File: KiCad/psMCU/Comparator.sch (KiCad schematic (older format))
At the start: 4 parts

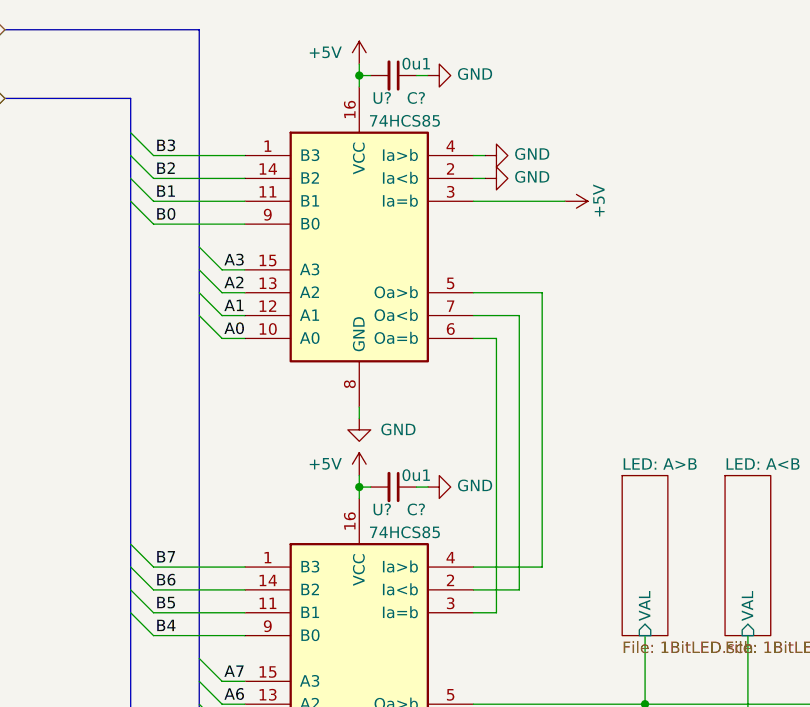
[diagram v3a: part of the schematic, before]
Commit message: Added some footprints, small optimisations
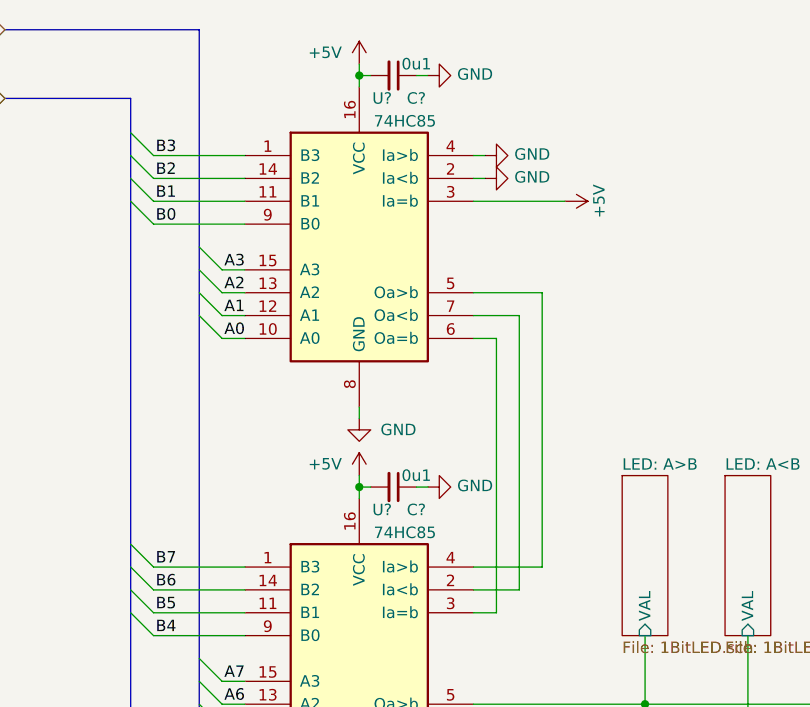
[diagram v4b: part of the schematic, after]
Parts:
- U? (x2): value 74HCS85 -> 74HC85; footprint (none) -> Package_SO:SOIC-16W_5.3x10.2mm_P1.27mm
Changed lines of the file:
@@
 AR Path="/5FD6B215/60020E04" Ref="U?"  Part="1"
 F 0 "U?" H 5600 4150 50  0000 C CNN
-F 1 "74HCS85" H 5700 4050 50  0000 C CNN
-F 2 "" H 5500 3500 50  0001 C CNN
+F 1 "74HC85" H 5700 4050 50  0000 C CNN
+F 2 "Package_SO:SOIC-16W_5.3x10.2mm_P1.27mm" H 5500 3500 50  0001 C CNN
 F 3 "http://www.ti.com/lit/gpn/sn74LS85" H 5500 3500 50  0001 C CNN
 	1    5500 3500
@@
 AR Path="/5FD6B215/60020521" Ref="U?"  Part="1"
 F 0 "U?" H 5600 2350 50  0000 C CNN
-F 1 "74HCS85" H 5700 2250 50  0000 C CNN
-F 2 "" H 5500 1700 50  0001 C CNN
+F 1 "74HC85" H 5700 2250 50  0000 C CNN
+F 2 "Package_SO:SOIC-16W_5.3x10.2mm_P1.27mm" H 5500 1700 50  0001 C CNN
 F 3 "http://www.ti.com/lit/gpn/sn74LS85" H 5500 1700 50  0001 C CNN
 	1    5500 1700

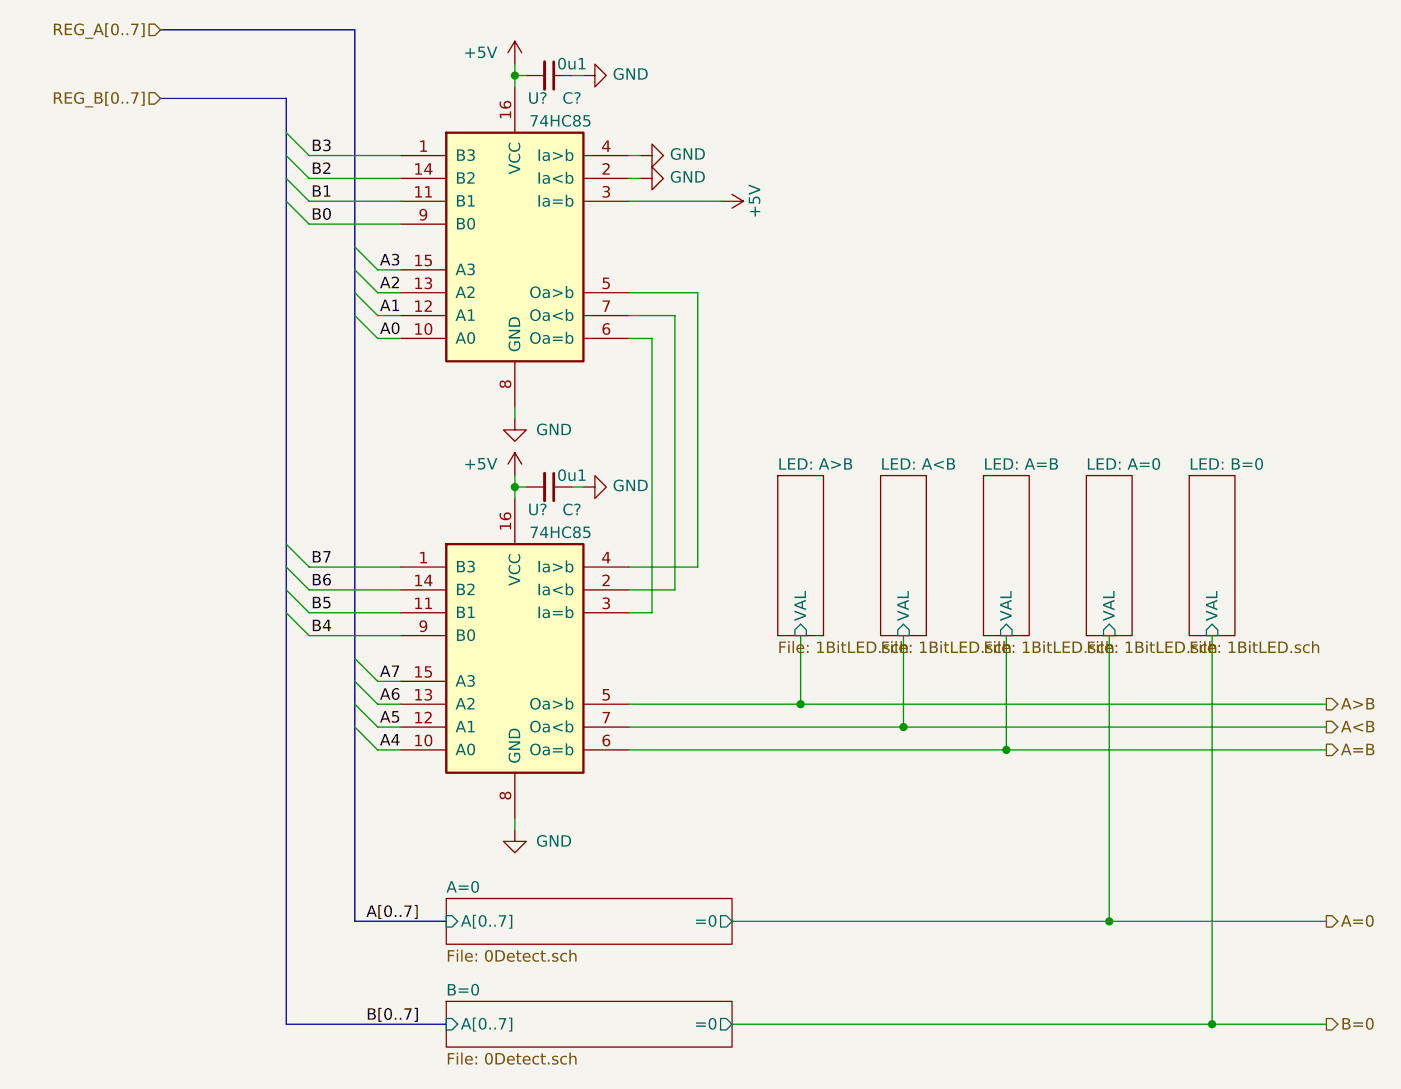
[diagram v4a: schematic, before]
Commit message: Removed Single LED sheets
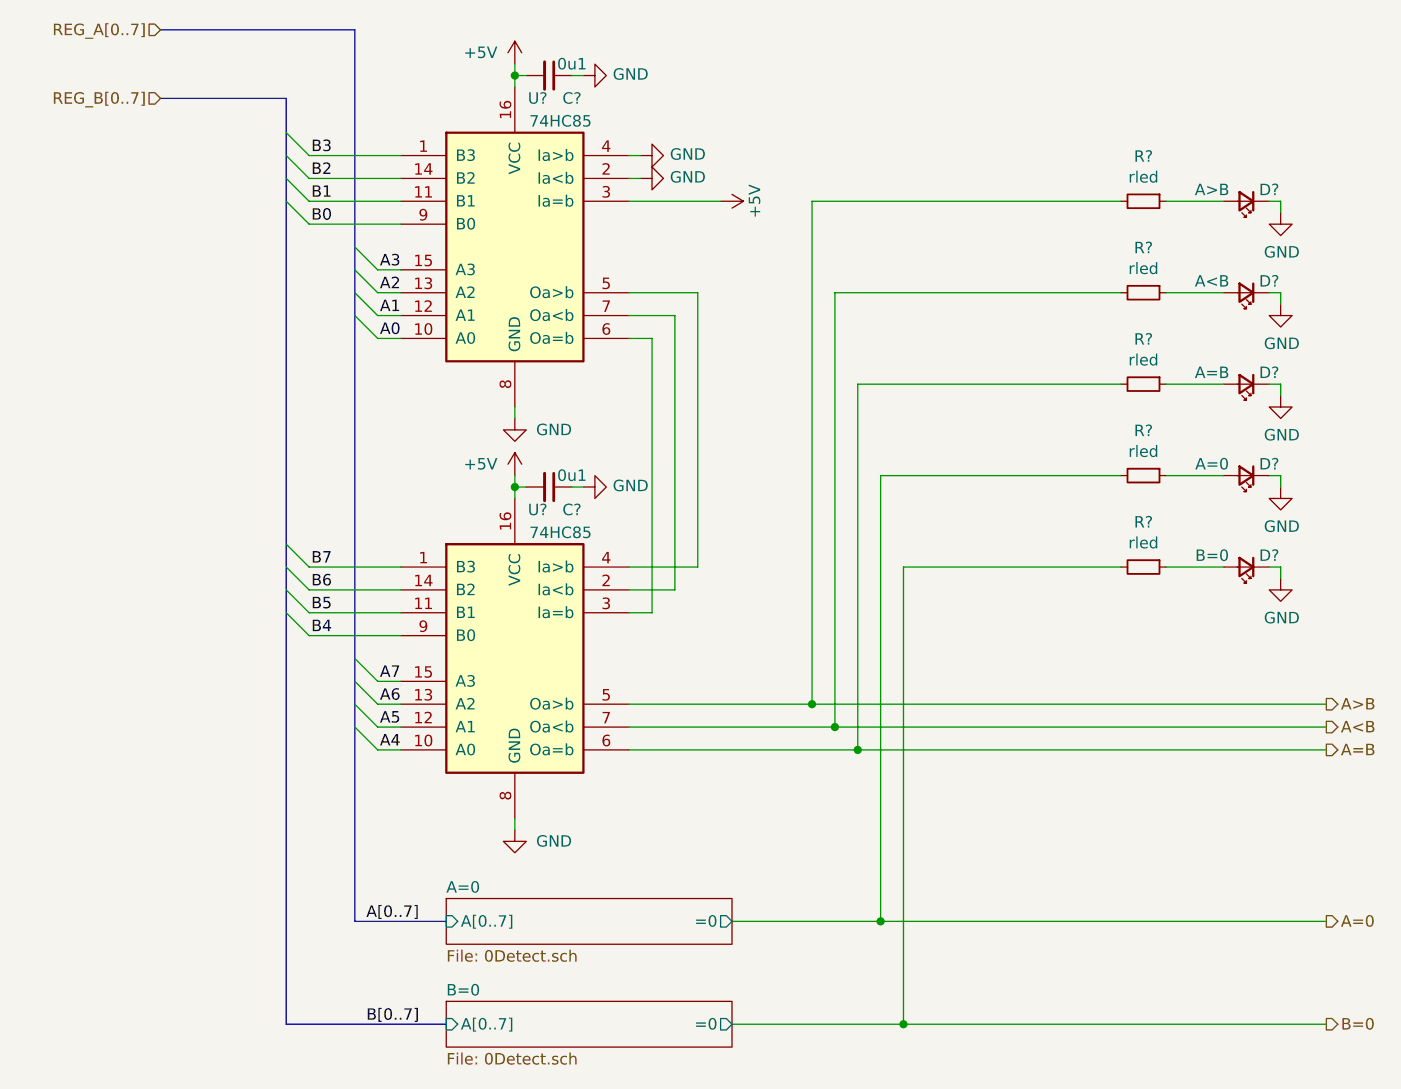
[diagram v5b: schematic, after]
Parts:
- added D?: A<B, Diode_SMD:D_0603_1608Metric, symbol Device:LED_Small
- added D?: A=B, Diode_SMD:D_0603_1608Metric, symbol Device:LED_Small
- added D?: A=0, Diode_SMD:D_0603_1608Metric, symbol Device:LED_Small
- added D?: B=0, Diode_SMD:D_0603_1608Metric, symbol Device:LED_Small
- added D?: A>B, Diode_SMD:D_0603_1608Metric, symbol Device:LED_Small
- added R? (x5): rled, Resistor_SMD:R_0603_1608Metric, symbol Device:R_Small
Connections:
- net A<B: now also R?.2
- net A=0: now also R?.2
- net A=B: now also R?.2
- net A>B: now also R?.2
- net B=0: now also R?.2
- net GND: now also D?.1 (K), D?.1 (K), D?.1 (K), D?.1 (K), D?.1 (K)
- new net: D?.2 (A), R?.1 (x5)

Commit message: First Schematic Draft done.
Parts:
- C210, C211: renamed from C?; footprint Capacitor_SMD:C_0603_1608Metric -> NoRef_Footprints:C_0603_1608Metric_NoRef
- D206, D207, D208, D209, D210: renamed from D?; footprint Diode_SMD:D_0603_1608Metric -> NoRef_Footprints:D_0603_1608Metric_NoRef
- R210, R211, R212, R213, R214: renamed from R?; footprint Resistor_SMD:R_0603_1608Metric -> NoRef_Footprints:R_0603_1608Metric
- gave numbers to parts that had none: 2

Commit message: Small improvements.
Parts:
- renumbered C210 to C208, C211 to C209, U210 to U208, U211 to U209
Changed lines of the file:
@@
 P 5500 900
 AR Path="/5F396002/60020527" Ref="#PWR?"  Part="1"
-AR Path="/5FD6B215/60020527" Ref="#PWR0921"  Part="1"
-F 0 "#PWR0921" H 5500 750 50  0001 C CNN
+AR Path="/5FD6B215/60020527" Ref="#PWR0906"  Part="1"
+F 0 "#PWR0906" H 5500 750 50  0001 C CNN
 F 1 "+5V" H 5350 950 50  0000 C CNN
 F 2 "" H 5500 900 50  0001 C CNN
@@
 AR Path="/5F1CE57C/6002052F" Ref="#PWR?"  Part="1"
 AR Path="/5F396002/6002052F" Ref="#PWR?"  Part="1"
-AR Path="/5FD6B215/6002052F" Ref="#PWR0925"  Part="1"
-F 0 "#PWR0925" H 5800 700 50  0001 C CNN
+AR Path="/5FD6B215/6002052F" Ref="#PWR0910"  Part="1"
+F 0 "#PWR0910" H 5800 700 50  0001 C CNN
 F 1 "GND" V 5805 822 50  0000 R CNN
 F 2 "" H 5800 950 50  0001 C CNN
@@
 AR Path="/5F1CE57C/60020535" Ref="C?"  Part="1"
 AR Path="/5F396002/60020535" Ref="C?"  Part="1"
-AR Path="/5FD6B215/60020535" Ref="C210"  Part="1"
-F 0 "C210" V 5750 1050 50  0000 C CNN
+AR Path="/5FD6B215/60020535" Ref="C208"  Part="1"
+F 0 "C208" V 5750 1050 50  0000 C CNN
 F 1 "0u1" V 5600 1050 50  0000 C CNN
 F 2 "NoRef_Footprints:C_0603_1608Metric_NoRef" H 5650 950 50  0001 C CNN
@@
 AR Path="/5F1CE57C/6002053E" Ref="#PWR?"  Part="1"
 AR Path="/5F396002/6002053E" Ref="#PWR?"  Part="1"
-AR Path="/5FD6B215/6002053E" Ref="#PWR0922"  Part="1"
-F 0 "#PWR0922" H 5500 2200 50  0001 C CNN
+AR Path="/5FD6B215/6002053E" Ref="#PWR0907"  Part="1"
+F 0 "#PWR0907" H 5500 2200 50  0001 C CNN
 F 1 "GND" H 5750 2400 50  0000 R CNN
 F 2 "" H 5500 2450 50  0001 C CNN
@@
 P 5500 3500
 AR Path="/5F396002/60020E04" Ref="U?"  Part="1"
-AR Path="/5FD6B215/60020E04" Ref="U211"  Part="1"
-F 0 "U211" H 5600 4150 50  0000 C CNN
+AR Path="/5FD6B215/60020E04" Ref="U209"  Part="1"
+F 0 "U209" H 5600 4150 50  0000 C CNN
 F 1 "74HC85" H 5700 4050 50  0000 C CNN
 F 2 "Package_SO:SOIC-16W_5.3x10.2mm_P1.27mm" H 5500 3500 50  0001 C CNN
@@
 P 5500 2700
 AR Path="/5F396002/60020E0A" Ref="#PWR?"  Part="1"
-AR Path="/5FD6B215/60020E0A" Ref="#PWR0923"  Part="1"
-F 0 "#PWR0923" H 5500 2550 50  0001 C CNN
+AR Path="/5FD6B215/60020E0A" Ref="#PWR0908"  Part="1"
+F 0 "#PWR0908" H 5500 2550 50  0001 C CNN
 F 1 "+5V" H 5350 2750 50  0000 C CNN
 F 2 "" H 5500 2700 50  0001 C CNN
@@
 AR Path="/5F1CE57C/60020E12" Ref="#PWR?"  Part="1"
 AR Path="/5F396002/60020E12" Ref="#PWR?"  Part="1"
-AR Path="/5FD6B215/60020E12" Ref="#PWR0926"  Part="1"
-F 0 "#PWR0926" H 5800 2500 50  0001 C CNN
+AR Path="/5FD6B215/60020E12" Ref="#PWR0911"  Part="1"
+F 0 "#PWR0911" H 5800 2500 50  0001 C CNN
 F 1 "GND" V 5805 2622 50  0000 R CNN
 F 2 "" H 5800 2750 50  0001 C CNN
@@
 AR Path="/5F1CE57C/60020E18" Ref="C?"  Part="1"
 AR Path="/5F396002/60020E18" Ref="C?"  Part="1"
-AR Path="/5FD6B215/60020E18" Ref="C211"  Part="1"
-F 0 "C211" V 5750 2850 50  0000 C CNN
+AR Path="/5FD6B215/60020E18" Ref="C209"  Part="1"
+F 0 "C209" V 5750 2850 50  0000 C CNN
 F 1 "0u1" V 5600 2850 50  0000 C CNN
 F 2 "NoRef_Footprints:C_0603_1608Metric_NoRef" H 5650 2750 50  0001 C CNN
@@
 AR Path="/5F1CE57C/60020E21" Ref="#PWR?"  Part="1"
 AR Path="/5F396002/60020E21" Ref="#PWR?"  Part="1"
-AR Path="/5FD6B215/60020E21" Ref="#PWR0924"  Part="1"
-F 0 "#PWR0924" H 5500 4000 50  0001 C CNN
+AR Path="/5FD6B215/60020E21" Ref="#PWR0909"  Part="1"
+F 0 "#PWR0909" H 5500 4000 50  0001 C CNN
 F 1 "GND" H 5750 4200 50  0000 R CNN
 F 2 "" H 5500 4250 50  0001 C CNN
@@
 AR Path="/5F1CE57C/600D374B" Ref="#PWR?"  Part="1"
 AR Path="/5F396002/600D374B" Ref="#PWR?"  Part="1"
-AR Path="/5FD6B215/600D374B" Ref="#PWR0927"  Part="1"
+AR Path="/5FD6B215/600D374B" Ref="#PWR0912"  Part="1"
 AR Path="/5FD6B215/60026810/600D374B" Ref="#PWR?"  Part="1"
-F 0 "#PWR0927" H 6050 1050 50  0001 C CNN
+F 0 "#PWR0912" H 6050 1050 50  0001 C CNN
 F 1 "GND" V 6055 1172 50  0000 R CNN
 F 2 "" H 6050 1300 50  0001 C CNN
@@
 AR Path="/5F1CE57C/600D3752" Ref="#PWR?"  Part="1"
 AR Path="/5F396002/600D3752" Ref="#PWR?"  Part="1"
-AR Path="/5FD6B215/600D3752" Ref="#PWR0928"  Part="1"
+AR Path="/5FD6B215/600D3752" Ref="#PWR0913"  Part="1"
 AR Path="/5FD6B215/60026810/600D3752" Ref="#PWR?"  Part="1"
-F 0 "#PWR0928" H 6050 1150 50  0001 C CNN
+F 0 "#PWR0913" H 6050 1150 50  0001 C CNN
 F 1 "GND" V 6055 1272 50  0000 R CNN
 F 2 "" H 6050 1400 50  0001 C CNN
@@
 P 6400 1500
 AR Path="/5F396002/600D3759" Ref="#PWR?"  Part="1"
-AR Path="/5FD6B215/600D3759" Ref="#PWR0929"  Part="1"
+AR Path="/5FD6B215/600D3759" Ref="#PWR0914"  Part="1"
 AR Path="/5FD6B215/60026810/600D3759" Ref="#PWR?"  Part="1"
-F 0 "#PWR0929" H 6400 1350 50  0001 C CNN
+F 0 "#PWR0914" H 6400 1350 50  0001 C CNN
 F 1 "+5V" H 6400 1650 50  0000 C CNN
 F 2 "" H 6400 1500 50  0001 C CNN
@@
 P 5500 1700
 AR Path="/5F396002/60020521" Ref="U?"  Part="1"
-AR Path="/5FD6B215/60020521" Ref="U210"  Part="1"
-F 0 "U210" H 5600 2350 50  0000 C CNN
+AR Path="/5FD6B215/60020521" Ref="U208"  Part="1"
+F 0 "U208" H 5600 2350 50  0000 C CNN
 F 1 "74HC85" H 5700 2250 50  0000 C CNN
 F 2 "Package_SO:SOIC-16W_5.3x10.2mm_P1.27mm" H 5500 1700 50  0001 C CNN
@@
 AR Path="/612C5E2A/62942D9E" Ref="#PWR?"  Part="1"
 AR Path="/5FD6EE9C/62942D9E" Ref="#PWR?"  Part="1"
-AR Path="/5FD6B215/62942D9E" Ref="#PWR0931"  Part="1"
-F 0 "#PWR0931" H 8850 1700 50  0001 C CNN
+AR Path="/5FD6B215/62942D9E" Ref="#PWR0916"  Part="1"
+F 0 "#PWR0916" H 8850 1700 50  0001 C CNN
 F 1 "GND" H 8855 1777 50  0000 C CNN
 F 2 "" H 8850 1950 50  0001 C CNN
@@
 AR Path="/612C5E2A/62943F8A" Ref="#PWR?"  Part="1"
 AR Path="/5FD6EE9C/62943F8A" Ref="#PWR?"  Part="1"
-AR Path="/5FD6B215/62943F8A" Ref="#PWR0932"  Part="1"
-F 0 "#PWR0932" H 8850 2100 50  0001 C CNN
+AR Path="/5FD6B215/62943F8A" Ref="#PWR0917"  Part="1"
+F 0 "#PWR0917" H 8850 2100 50  0001 C CNN
 F 1 "GND" H 8855 2177 50  0000 C CNN
 F 2 "" H 8850 2350 50  0001 C CNN
@@
 AR Path="/612C5E2A/62944E75" Ref="#PWR?"  Part="1"
 AR Path="/5FD6EE9C/62944E75" Ref="#PWR?"  Part="1"
-AR Path="/5FD6B215/62944E75" Ref="#PWR0933"  Part="1"
-F 0 "#PWR0933" H 8850 2500 50  0001 C CNN
+AR Path="/5FD6B215/62944E75" Ref="#PWR0918"  Part="1"
+F 0 "#PWR0918" H 8850 2500 50  0001 C CNN
 F 1 "GND" H 8855 2577 50  0000 C CNN
 F 2 "" H 8850 2750 50  0001 C CNN
@@
 AR Path="/612C5E2A/629461A5" Ref="#PWR?"  Part="1"
 AR Path="/5FD6EE9C/629461A5" Ref="#PWR?"  Part="1"
-AR Path="/5FD6B215/629461A5" Ref="#PWR0934"  Part="1"
-F 0 "#PWR0934" H 8850 2900 50  0001 C CNN
+AR Path="/5FD6B215/629461A5" Ref="#PWR0919"  Part="1"
+F 0 "#PWR0919" H 8850 2900 50  0001 C CNN
 F 1 "GND" H 8855 2977 50  0000 C CNN
 F 2 "" H 8850 3150 50  0001 C CNN
@@
 AR Path="/612C5E2A/62947FB0" Ref="#PWR?"  Part="1"
 AR Path="/5FD6EE9C/62947FB0" Ref="#PWR?"  Part="1"
-AR Path="/5FD6B215/62947FB0" Ref="#PWR0930"  Part="1"
-F 0 "#PWR0930" H 8850 1300 50  0001 C CNN
+AR Path="/5FD6B215/62947FB0" Ref="#PWR0915"  Part="1"
+F 0 "#PWR0915" H 8850 1300 50  0001 C CNN
 F 1 "GND" H 8855 1377 50  0000 C CNN
 F 2 "" H 8850 1550 50  0001 C CNN

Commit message: Cleanup, ready for specific component values.
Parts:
- U208, U209: footprint Package_SO:SOIC-16W_5.3x10.2mm_P1.27mm -> Package_SO:SOIC-16_3.9x9.9mm_P1.27mm
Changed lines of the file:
@@
 $Descr A4 11693 8268
 encoding utf-8
-Sheet 53 113
+Sheet 53 110
 Title "psMCU"
 Date ""
@@
 F 0 "U209" H 5600 4150 50  0000 C CNN
 F 1 "74HC85" H 5700 4050 50  0000 C CNN
-F 2 "Package_SO:SOIC-16W_5.3x10.2mm_P1.27mm" H 5500 3500 50  0001 C CNN
+F 2 "Package_SO:SOIC-16_3.9x9.9mm_P1.27mm" H 5500 3500 50  0001 C CNN
 F 3 "http://www.ti.com/lit/gpn/sn74LS85" H 5500 3500 50  0001 C CNN
 	1    5500 3500
@@
 F 0 "U208" H 5600 2350 50  0000 C CNN
 F 1 "74HC85" H 5700 2250 50  0000 C CNN
-F 2 "Package_SO:SOIC-16W_5.3x10.2mm_P1.27mm" H 5500 1700 50  0001 C CNN
+F 2 "Package_SO:SOIC-16_3.9x9.9mm_P1.27mm" H 5500 1700 50  0001 C CNN
 F 3 "http://www.ti.com/lit/gpn/sn74LS85" H 5500 1700 50  0001 C CNN
 	1    5500 1700
